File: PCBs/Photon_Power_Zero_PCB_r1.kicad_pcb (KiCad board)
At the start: 2 copper layers, 30.1 x 65.1 mm, 56 parts, among them J1 JST_S2B-PH-SM4-TB_LF__SN_, J2 JST_GH_SM02B-GHS-TB_1x02-1MP_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, J3 SMT_Solar_barrel, U1 ATtiny84-SSFR, U2 REG_MCP1700T-3602E/MB, U3 bq2407, U4 AP2161-WG, U5 TPS613222A

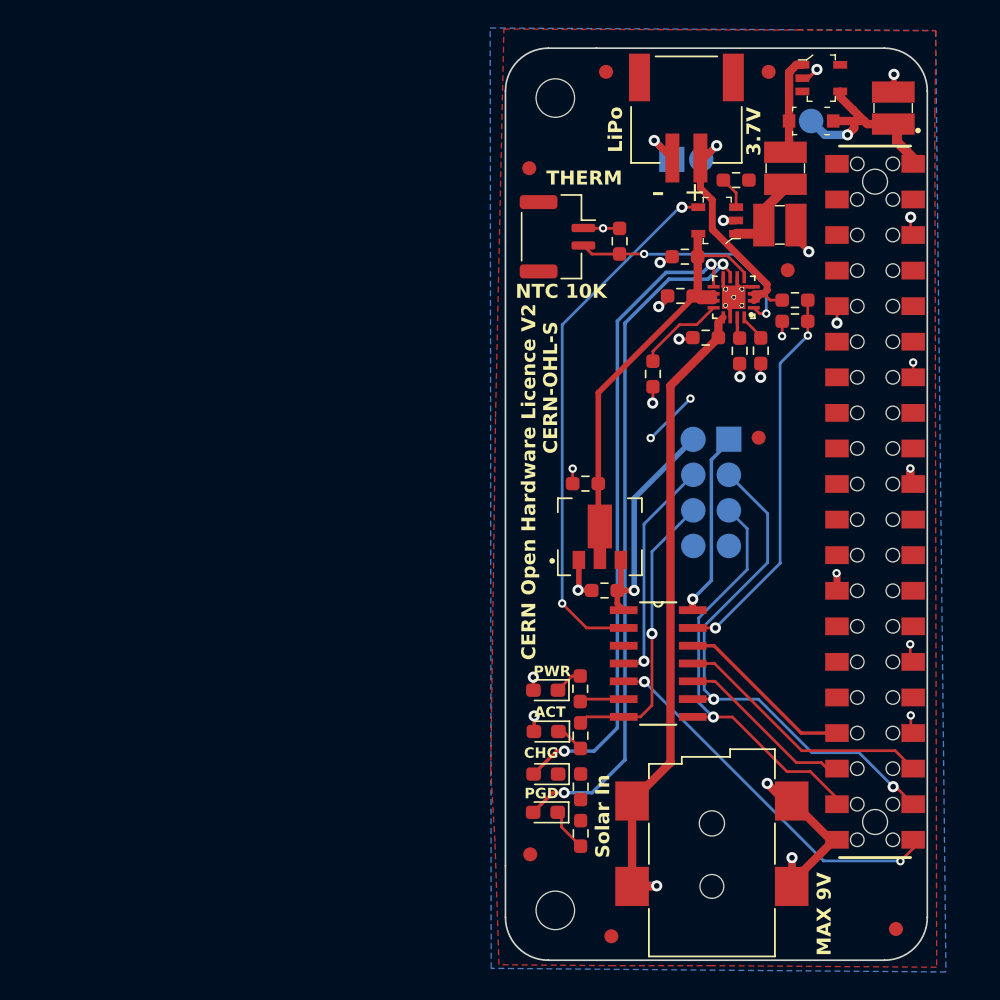
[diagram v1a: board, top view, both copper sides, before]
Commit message: Rotated PCB
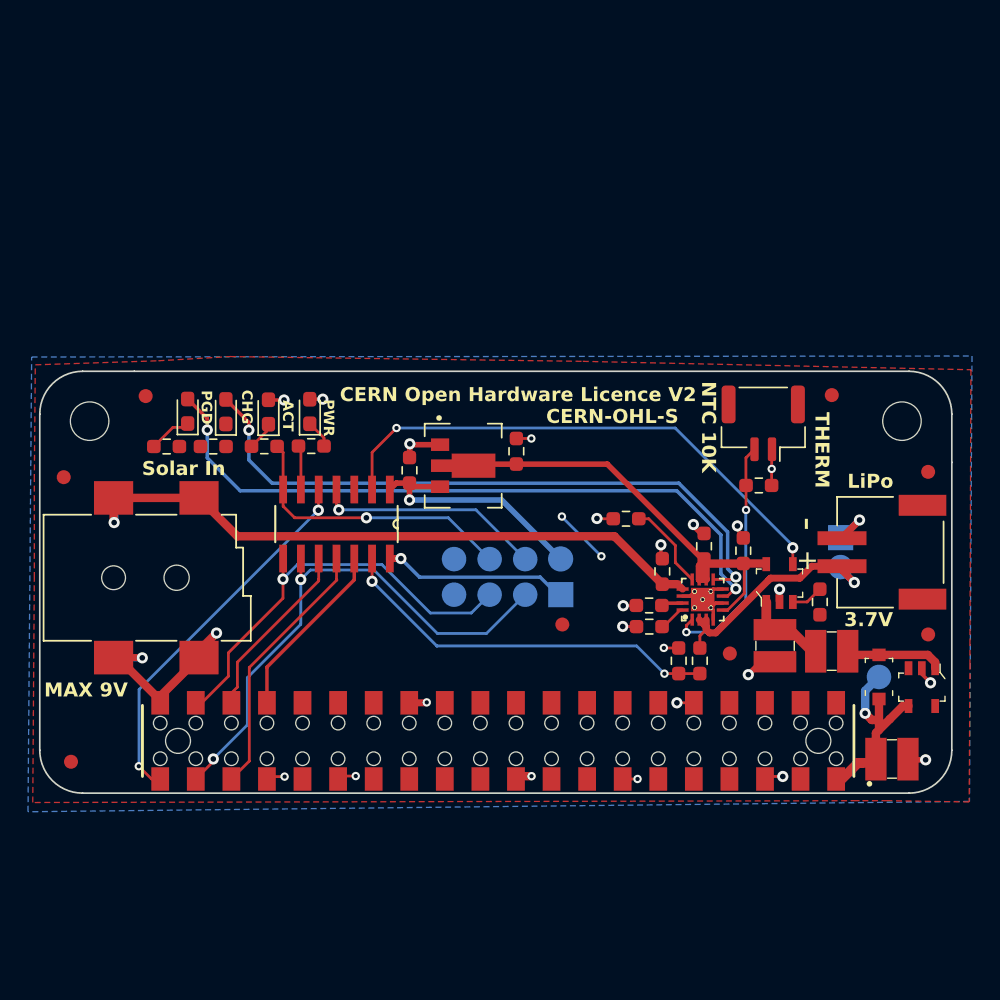
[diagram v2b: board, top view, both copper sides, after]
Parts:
- moved FID4 60.1 mm to (123.8, 125.4), turned to -90 degrees
- moved REF** 51.1 mm to (126.8, 117.9), turned to 90 degrees
- moved FID5 51.0 mm to (123.2, 105.0), turned to -90 degrees
- moved C3 46.5 mm to (182.4, 125.2), turned to 0 degrees
- moved ? 46.3 mm to (126.7, 106.5), turned to -90 degrees
- moved U5 44.1 mm to (184.5, 120.0), turned to 180 degrees
- moved FID6 42.7 mm to (129.1, 99.3), turned to -90 degrees
- moved FID2 41.8 mm to (185.0, 116.3), turned to -90 degrees
- moved R2 40.5 mm to (130.6, 102.9), turned to 0 degrees
- moved ? 40.0 mm to (181.4, 119.3), turned to -90 degrees
- moved D2 40.0 mm to (181.4, 119.3), turned to 90 degrees
- moved D1 38.4 mm to (132.1, 100.3), turned to 90 degrees
- moved J3 37.7 mm to (132.9, 106.5), turned to 0 degrees
- moved FID1 36.7 mm to (185.0, 104.7), turned to -90 degrees
- moved R2 35.8 mm to (133.9, 102.9), turned to 180 degrees
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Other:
- board size 30.1 x 65.1 mm -> 65.1 x 30.1 mm
